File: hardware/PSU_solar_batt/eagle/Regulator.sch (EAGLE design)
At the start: 28 parts, among them IC1 MCP3550-60MS, IC2 MCP3550-60MS, IC3 MCP73831/OT

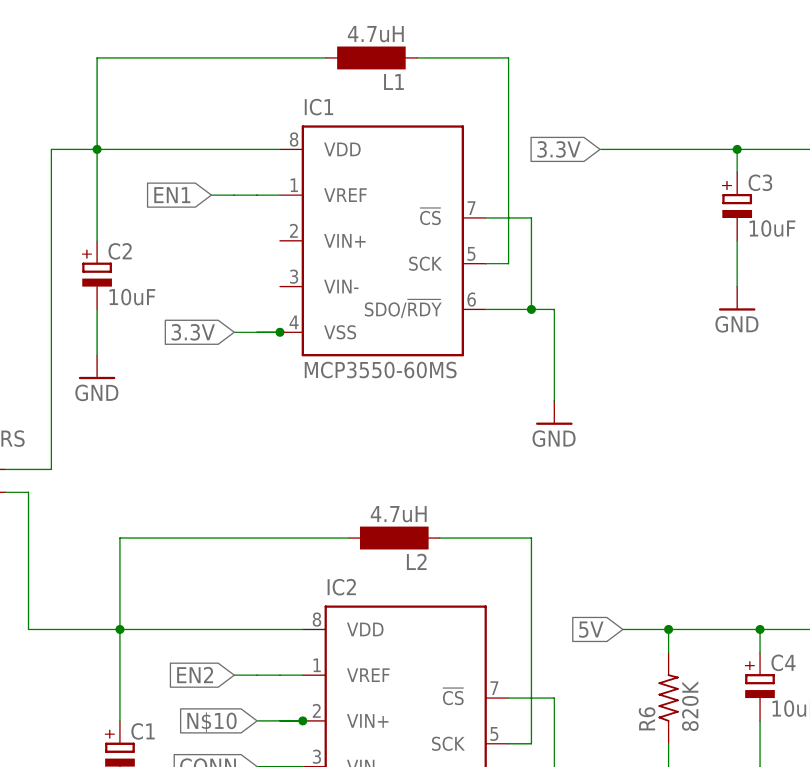
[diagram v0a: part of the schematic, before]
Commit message: renames IC1 and IC2 to MCP1642 to avoid confusion (currently MCP3550 part is used instead because MCP1642 is not in the Microchip library)
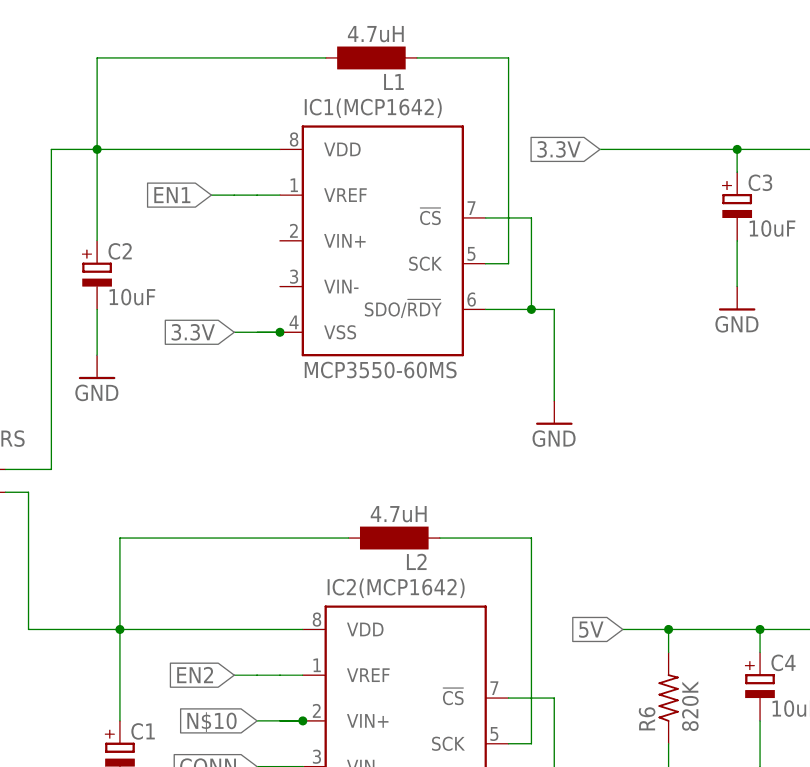
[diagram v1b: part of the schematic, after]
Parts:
- renumbered IC1 to IC1(MCP1642), IC2 to IC2(MCP1642)
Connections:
- net N$1 renamed MCP1642
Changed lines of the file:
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@@
 <?xml version="1.0" encoding="utf-8"?>
 <!DOCTYPE eagle SYSTEM "eagle.dtd">
-<eagle version="7.2.0">
+<eagle version="7.1.0">
 <drawing>
 <settings>
@@
 <part name="GND12" library="supply1" deviceset="GND" device=""/>
 <part name="GND13" library="supply1" deviceset="GND" device=""/>
-<part name="IC1" library="microchip" deviceset="MCP355*" device="MS" technology="0-60"/>
+<part name="IC1(MCP1642)" library="microchip" deviceset="MCP355*" device="MS" technology="0-60"/>
 <part name="L2" library="inductor-neosid" deviceset="MS85" device="" value="4.7uH"/>
 <part name="C1" library="rcl" deviceset="CPOL-EU" device="140CLH-1010" value="10uF"/>
@@
 <part name="5VOUT1" library="con-wago-508" deviceset="W237-02P" device=""/>
 <part name="GND7" library="supply1" deviceset="GND" device=""/>
-<part name="IC2" library="microchip" deviceset="MCP355*" device="MS" technology="0-60"/>
+<part name="IC2(MCP1642)" library="microchip" deviceset="MCP355*" device="MS" technology="0-60"/>
 <part name="GND8" library="supply1" deviceset="GND" device=""/>
 <part name="R6" library="adafruit" deviceset="R-US_" device="M0805" value="820K"/>
@@
 <instance part="GND12" gate="1" x="-129.54" y="-17.78"/>
 <instance part="GND13" gate="1" x="68.58" y="63.5"/>
-<instance part="IC1" gate="-1" x="15.24" y="66.04"/>
+<instance part="IC1(MCP1642)" gate="-1" x="15.24" y="66.04"/>
 <instance part="L2" gate="G$1" x="17.78" y="33.02" rot="R180"/>
 <instance part="C1" gate="G$1" x="-12.7" y="10.16"/>
@@
 <instance part="5VOUT1" gate="-2" x="81.28" y="20.32" rot="R180"/>
 <instance part="GND7" gate="1" x="71.12" y="10.16"/>
-<instance part="IC2" gate="-1" x="17.78" y="12.7"/>
+<instance part="IC2(MCP1642)" gate="-1" x="17.78" y="12.7"/>
 <instance part="GND8" gate="1" x="48.26" y="-48.26"/>
 <instance part="R6" gate="G$1" x="48.26" y="15.24" rot="R90"/>
@@
 </busses>
 <nets>
-<net name="N$1" class="0">
+<net name="MCP1642" class="0">
 <segment>
 <pinref part="C2" gate="G$1" pin="+"/>
@@
 <wire x1="-20.32" y1="40.64" x2="-20.32" y2="76.2" width="0.1524" layer="91"/>
 <junction x="-15.24" y="76.2"/>
-<pinref part="IC1" gate="-1" pin="VDD"/>
+<pinref part="IC1(MCP1642)" gate="-1" pin="VDD"/>
 </segment>
 </net>
@@
 </segment>
 <segment>
-<pinref part="IC1" gate="-1" pin="!CS"/>
+<pinref part="IC1(MCP1642)" gate="-1" pin="!CS"/>
 <wire x1="27.94" y1="68.58" x2="33.02" y2="68.58" width="0.1524" layer="91"/>
 <wire x1="33.02" y1="68.58" x2="33.02" y2="58.42" width="0.1524" layer="91"/>
@@
 <wire x1="33.02" y1="58.42" x2="35.56" y2="58.42" width="0.1524" layer="91"/>
 <wire x1="35.56" y1="58.42" x2="35.56" y2="48.26" width="0.1524" layer="91"/>
-<pinref part="IC1" gate="-1" pin="SDO/!RDY"/>
+<pinref part="IC1(MCP1642)" gate="-1" pin="SDO/!RDY"/>
 <wire x1="27.94" y1="58.42" x2="33.02" y2="58.42" width="0.1524" layer="91"/>
 <junction x="33.02" y="58.42"/>
@@
 </segment>
 <segment>
-<pinref part="IC2" gate="-1" pin="!CS"/>
+<pinref part="IC2(MCP1642)" gate="-1" pin="!CS"/>
 <wire x1="30.48" y1="15.24" x2="35.56" y2="15.24" width="0.1524" layer="91"/>
 <wire x1="35.56" y1="15.24" x2="35.56" y2="5.08" width="0.1524" layer="91"/>
@@
 <wire x1="35.56" y1="5.08" x2="38.1" y2="5.08" width="0.1524" layer="91"/>
 <wire x1="38.1" y1="5.08" x2="38.1" y2="-5.08" width="0.1524" layer="91"/>
-<pinref part="IC2" gate="-1" pin="SDO/!RDY"/>
+<pinref part="IC2(MCP1642)" gate="-1" pin="SDO/!RDY"/>
 <wire x1="30.48" y1="5.08" x2="35.56" y2="5.08" width="0.1524" layer="91"/>
 <junction x="35.56" y="5.08"/>
@@
 <wire x1="-22.86" y1="22.86" x2="-12.7" y2="22.86" width="0.1524" layer="91"/>
 <junction x="-12.7" y="22.86"/>
-<pinref part="IC2" gate="-1" pin="VDD"/>
+<pinref part="IC2(MCP1642)" gate="-1" pin="VDD"/>
 </segment>
 </net>
@@
 <net name="3.3V" class="0">
 <segment>
-<pinref part="IC1" gate="-1" pin="VSS"/>
+<pinref part="IC1(MCP1642)" gate="-1" pin="VSS"/>
 <wire x1="5.08" y1="55.88" x2="2.54" y2="55.88" width="0.1524" layer="91"/>
 <label x="0" y="55.88" size="1.778" layer="95" rot="R180" xref="yes"/>
@@
 <wire x1="20.32" y1="86.36" x2="30.48" y2="86.36" width="0.1524" layer="91"/>
 <wire x1="30.48" y1="86.36" x2="30.48" y2="63.5" width="0.1524" layer="91"/>
-<pinref part="IC1" gate="-1" pin="SCK"/>
+<pinref part="IC1(MCP1642)" gate="-1" pin="SCK"/>
 <wire x1="30.48" y1="63.5" x2="27.94" y2="63.5" width="0.1524" layer="91"/>
 </segment>
@@
 <wire x1="22.86" y1="33.02" x2="33.02" y2="33.02" width="0.1524" layer="91"/>
 <wire x1="33.02" y1="33.02" x2="33.02" y2="10.16" width="0.1524" layer="91"/>
-<pinref part="IC2" gate="-1" pin="SCK"/>
+<pinref part="IC2(MCP1642)" gate="-1" pin="SCK"/>
 <wire x1="33.02" y1="10.16" x2="30.48" y2="10.16" width="0.1524" layer="91"/>
 </segment>
@@
 <net name="5V" class="0">
 <segment>
-<pinref part="IC2" gate="-1" pin="VSS"/>
+<pinref part="IC2(MCP1642)" gate="-1" pin="VSS"/>
 <wire x1="7.62" y1="2.54" x2="5.08" y2="2.54" width="0.1524" layer="91"/>
 <label x="-2.54" y="2.54" size="1.778" layer="95" rot="R180" xref="yes"/>
@@
 <net name="N$10" class="0">
 <segment>
-<pinref part="IC2" gate="-1" pin="VIN+"/>
+<pinref part="IC2(MCP1642)" gate="-1" pin="VIN+"/>
 <wire x1="7.62" y1="12.7" x2="5.08" y2="12.7" width="0.1524" layer="91"/>
 <label x="2.54" y="12.7" size="1.778" layer="95" rot="R180" xref="yes"/>
@@
 <net name="CONN" class="0">
 <segment>
-<pinref part="IC2" gate="-1" pin="VIN-"/>
+<pinref part="IC2(MCP1642)" gate="-1" pin="VIN-"/>
 <wire x1="5.08" y1="7.62" x2="7.62" y2="7.62" width="0.1524" layer="91"/>
 <label x="2.54" y="7.62" size="1.778" layer="95" rot="R180" xref="yes"/>
@@
 <net name="EN1" class="0">
 <segment>
-<pinref part="IC1" gate="-1" pin="VREF"/>
+<pinref part="IC1(MCP1642)" gate="-1" pin="VREF"/>
 <wire x1="5.08" y1="71.12" x2="2.54" y2="71.12" width="0.1524" layer="91"/>
 <label x="-2.54" y="71.12" size="1.778" layer="95" rot="R180" xref="yes"/>
@@
 <net name="EN2" class="0">
 <segment>
-<pinref part="IC2" gate="-1" pin="VREF"/>
+<pinref part="IC2(MCP1642)" gate="-1" pin="VREF"/>
 <wire x1="7.62" y1="17.78" x2="5.08" y2="17.78" width="0.1524" layer="91"/>
 <label x="0" y="17.78" size="1.778" layer="95" rot="R180" xref="yes"/>
